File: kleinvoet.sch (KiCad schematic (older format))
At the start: 36 parts, among them J1 Conn_ST_STDC14, SW1 RESET, SW2 USER, U1 STM32F446RETx, U2 NOR Flash, Y1 12 MHz, Y2 32.768 kHz

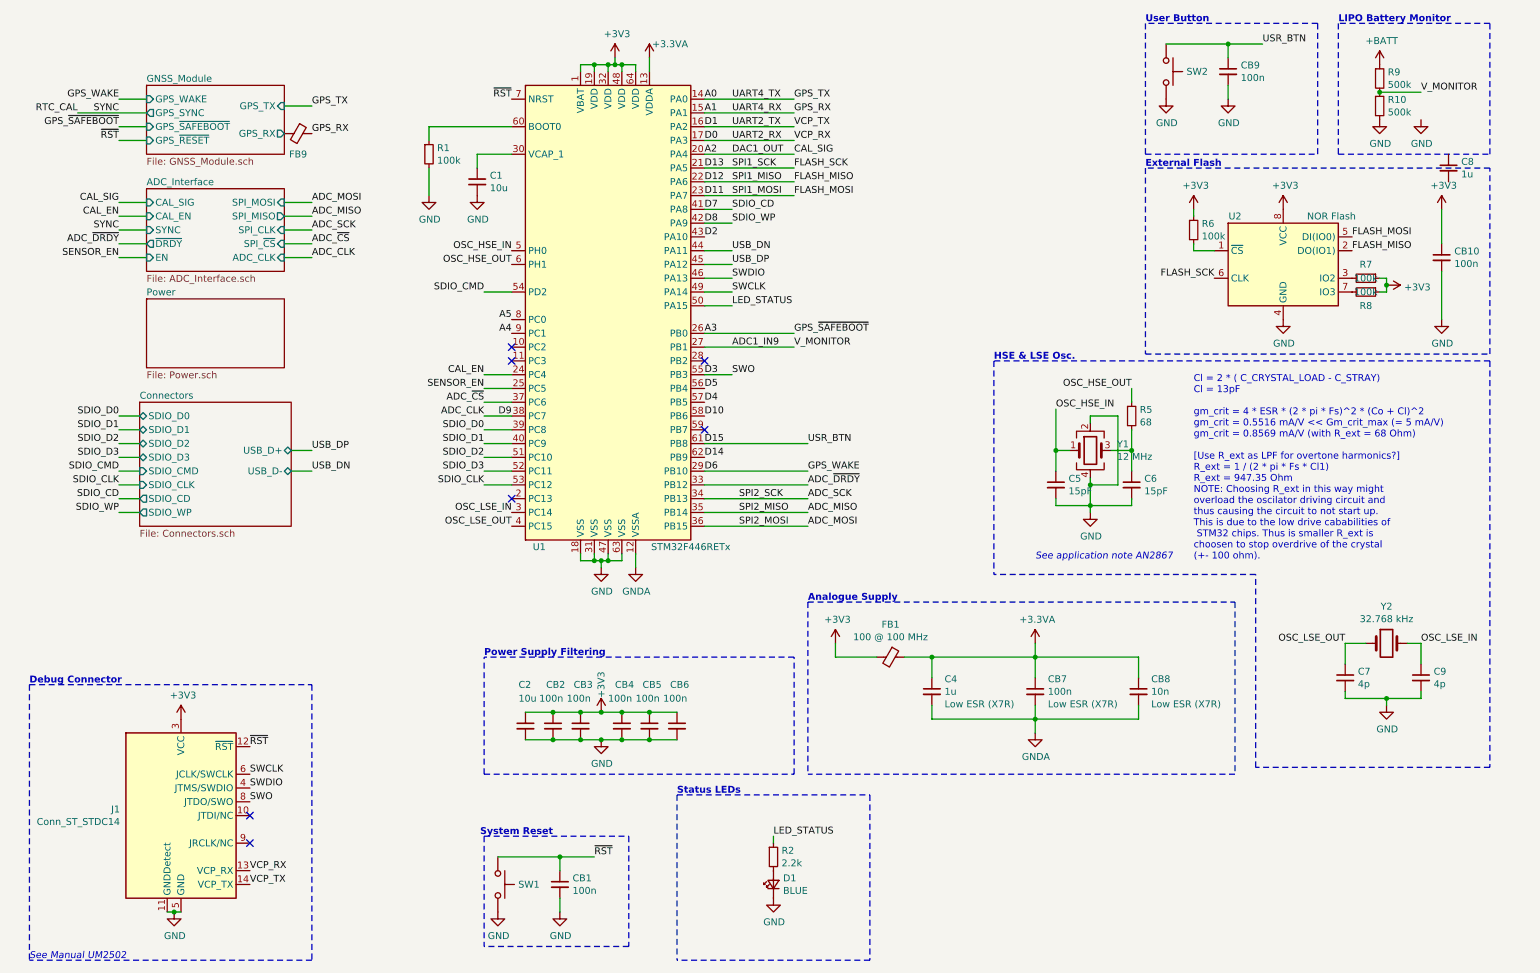
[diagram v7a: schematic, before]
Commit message: New ADC board layout
Merge feature/kv-new-adc

Squashed commit of the following:
===============================================

commit d560af3129baffdc71a13a7fa7beda6d7e4b1bbe
Author: CM Geldenhuys <20198329@sun.ac.za>
Date:   Mon Nov 2 10:16:05 2020 +0200

    Change board layout

commit e0e102b1b715915958904bd07514080422fcc802
Author: CM Geldenhuys <20198329@sun.ac.za>
Date:   Mon Nov 2 08:42:49 2020 +0200

    Route ADC rst

commit dbc5adba55d665b163eedfb4150514fe2b5b8ec8
Author: CM Geldenhuys <20198329@sun.ac.za>
Date:   Mon Nov 2 08:37:27 2020 +0200

    Fix GPS conn.

commit 0f139c20ac4bbbbfd2ab5507f187a5ddf70be7a1
Author: CM Geldenhuys <20198329@sun.ac.za>
Date:   Mon Nov 2 08:23:01 2020 +0200

    Route USR BTN

commit f6bd16c8e79a9fc3047a82e3e1abb388a579a1e4
Author: CM Geldenhuys <20198329@sun.ac.za>
Date:   Sun Nov 1 07:41:20 2020 +0200

    Route GPS Conn

commit 016e6e7ba1ce602e3233b00102ced6621a380f78
Author: CM Geldenhuys <20198329@sun.ac.za>
Date:   Fri Oct 30 17:31:13 2020 +0200

    Route Misc.

commit 6a809ae2e129821f12cca4ec3806ebf69337c268
Author: CM Geldenhuys <20198329@sun.ac.za>
Date:   Fri Oct 30 11:40:29 2020 +0200

    (WIP) SD config

commit b5d79f248cd283a71c5ab746a4afc4eb96850216
Author: CM Geldenhuys <20198329@sun.ac.za>
Date:   Fri Oct 30 11:24:56 2020 +0200

    Route ST-Link

commit dba35a7554c0c60ddd581dd4b7cbdf28445f26a1
Author: CM Geldenhuys <20198329@sun.ac.za>
Date:   Fri Oct 30 11:03:44 2020 +0200

    Route out GND planes

commit ee78e0f947a8edc358d3e2ec17c7ddf8f87e82dd
Author: CM Geldenhuys <20198329@sun.ac.za>
Date:   Thu Oct 29 16:17:03 2020 +0200

    Change ST-LINk loc.

commit b281a3fe16ed9d80db1964422c72eaf6acbfd9f3
Author: CM Geldenhuys <20198329@sun.ac.za>
Date:   Thu Oct 29 15:43:37 2020 +0200

    Major layout update

commit 655eae6cd0c7e79d683f16c4706ab989a6952fc5
Author: CM Geldenhuys <20198329@sun.ac.za>
Date:   Thu Oct 29 12:05:26 2020 +0200

    Route analog section

commit 0aa4140e89fcb36b0e9f339e25cad0a47a5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
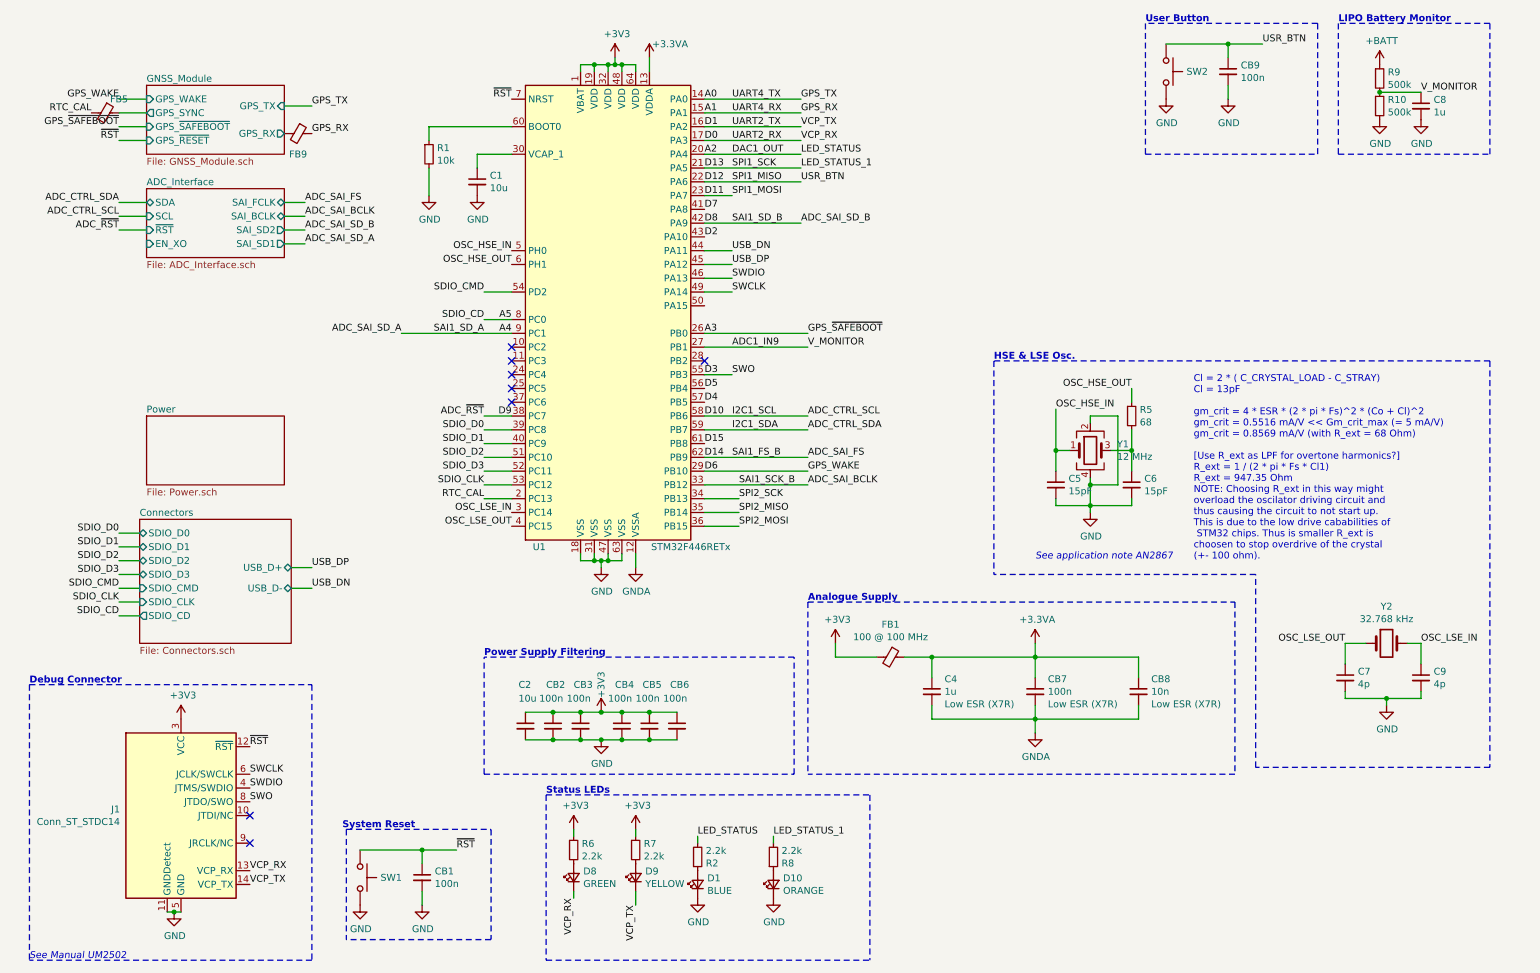
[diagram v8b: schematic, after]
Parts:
- removed CB10: 100n, Capacitor_SMD:C_0603_1608Metric_Pad1.08x0.95mm_HandSolder, symbol Device:C_Small
- removed U2: NOR Flash, grootvoet:SOIC-8_5.23x5.23mm_P1.27mm, symbol Memory_Flash:W25Q128JVS
- added D10: ORANGE, LED_SMD:LED_0603_1608Metric_Pad1.05x0.95mm_HandSolder, symbol Device:LED_Small
- added D8: GREEN, LED_SMD:LED_0603_1608Metric_Pad1.05x0.95mm_HandSolder, symbol Device:LED_Small
- added D9: YELLOW, LED_SMD:LED_0603_1608Metric_Pad1.05x0.95mm_HandSolder, symbol Device:LED_Small
- added FB5: BLM15HD102SN1, Inductor_SMD:L_0402_1005Metric, symbol Device:Ferrite_Bead_Small
- C1, C2: footprint Capacitor_SMD:C_0805_2012Metric_Pad1.15x1.40mm_HandSolder -> Capacitor_SMD:C_0805_2012Metric_Pad1.18x1.45mm_HandSolder
- J1: footprint grootvoet:SAMTEC-FTSH-107-01-X-D -> grootvoet:SAMTEC-FTSH-107-01-X-DV; MPN M50-055023W0445 -> FTSH-107-01-F-DV-K; Mfr. Harwin -> Samtec
- R1: value 100k -> 10k; footprint Resistor_SMD:R_0603_1608Metric_Pad1.05x0.95mm_HandSolder -> Resistor_SMD:R_0603_1608Metric_Pad0.98x0.95mm_HandSolder; MPN RC0603FR-07100KL -> (none)
- R10, R2, R5, R9: footprint Resistor_SMD:R_0603_1608Metric_Pad1.05x0.95mm_HandSolder -> Resistor_SMD:R_0603_1608Metric_Pad0.98x0.95mm_HandSolder
- R6, R7, R8: value 100k -> 2.2k; footprint Resistor_SMD:R_0603_1608Metric_Pad1.05x0.95mm_HandSolder -> Resistor_SMD:R_0603_1608Metric_Pad0.98x0.95mm_HandSolder; MPN RC0603FR-07100KL -> RC0603FR-072K2L
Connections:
- net +3V3: no longer R8.1
- net A2: now also R2.2
- net ADC1_IN9: now also C8.1
- net D0: now also D8.1 (K)
- net D1: now also D9.1 (K)
- net D12: now also CB9.1, SW2.1
- net D13: now also R8.2
- net D15: no longer CB9.1, SW2.1
- net GND: now also C8.2, D10.1 (K)
- net RTC_CAL: now also U1.2 (PC13), FB5.2
- net at R6.2: now also D8.2 (A)
- net at R7.2: now also D9.2 (A)
- net at D1.2 (A): now also R2.1; no longer R2.2
- net ADC_CTRL_SDA: now reaches U1.59 (PB7)
- net ADC_CLK renamed ADC_~RST
- net ADC_MISO renamed SPI2_MISO
- net ADC_MOSI renamed SPI2_MOSI
- net ADC_SCK renamed SPI2_SCK
- net ADC_~CS: no longer names the net of U1.37 (PC6)
- net ADC_~DRDY renamed ADC_SAI_BCLK
- net CAL_EN: no longer names the net of U1.24 (PC4)
- net D10 renamed ADC_CTRL_SCL
- net D14 renamed ADC_SAI_FS
- net D8 renamed ADC_SAI_SD_B
- net LED_STATUS: no longer names the net of U1.50 (PA15)
- net LED_STATUS: no longer R2.1
- net SENSOR_EN: no longer names the net of U1.25 (PC5)
- new net: D10.2 (A), R8.1
- new net GNSS_Module/GPS_SYNC: FB5.1
- no-connect marks 7 -> 8
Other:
- note removed: "External Flash"
- moved on the sheet: C8, CB1, D1, R2, SW1
